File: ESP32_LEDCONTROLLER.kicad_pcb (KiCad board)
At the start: 2 copper layers, 17 parts, among them J1 ST-04, J2 ST-00, J3 ST-01, J4 ST-02, J5 ST-03, U1 LM2576HVT-5, U2 ESP32_NODEMCU

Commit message: v0.1 of the LED Controller has been completed.
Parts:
- added D1: D_Schottky, Diode_THT:D_DO-27_P12.70mm_Horizontal, F.Cu at (144.8, 109.2)
- added L1: L100, Inductor_THT:L_Radial_D9.5mm_P5.00mm_Fastron_07HVP, F.Cu at (134.6, 91.4)
- added U3: SN74LV4T125, Package_DIP:DIP-14_W7.62mm, F.Cu at (83.8, 110.5)
- C2: footprint Capacitor_THT:CP_Radial_D8.0mm_P3.50mm -> Capacitor_THT:CP_Radial_D10.0mm_P5.00mm
- R1, R2, R3, R4, R5, R6, R7, R8: footprint Resistor_THT:R_Axial_DIN0207_L6.3mm_D2.5mm_P2.54mm_Vertical -> Resistor_THT:R_Axial_DIN0207_L6.3mm_D2.5mm_P7.62mm_Horizontal
- U2: value ESP32_NODEMCU -> ESP32-DEVKIT-V1; footprint Esp32NodeMCU:MODULE_ESP32_NODEMCU -> ESP32-Devkitv1:MODULE_ESP32_DEVKIT_V1
- moved J5 161.1 mm to (85.1, 127.0), turned to -90 degrees
- moved J4 155.3 mm to (85.1, 116.8), turned to -90 degrees
- moved R7 131.8 mm to (99.1, 127.0), turned to 180 degrees
- moved R8 129.3 mm to (99.1, 132.1), turned to 180 degrees
- moved R5 128.5 mm to (99.1, 116.8), turned to 180 degrees
- moved R6 125.0 mm to (99.1, 121.9), turned to 180 degrees
- moved U2 88.7 mm to (116.8, 111.8), turned to 180 degrees
- moved J2 87.6 mm to (156.2, 132.1), turned to 90 degrees
- moved R2 86.2 mm to (142.2, 127.0)
- moved R3 86.2 mm to (142.2, 121.9)
- moved J3 85.6 mm to (156.2, 121.9)
- moved R1 83.6 mm to (142.2, 132.1)
- moved R4 80.7 mm to (142.2, 116.8)
- moved C2 46.8 mm to (139.7, 104.1)
- moved U1 30.6 mm to (147.3, 99.1), turned to 90 degrees
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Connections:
- R1 pad 1: Net-(U2-PadJ5_4) -> Net-(R1-Pad1)
- R2 pad 1: Net-(U2-PadJ5_2) -> Net-(R2-Pad1)
- R3 pad 1: Net-(U2-PadJ4_14) -> Net-(R3-Pad1)
- R4 pad 1: Net-(U2-PadJ4_13) -> Net-(R4-Pad1)
- U1 pad 2: VCC -> Net-(D1-Pad1)
- U1 pad 4: unconnected-(U1-Pad4) -> VCC
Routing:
- net VCC: track 0.00 -> 156.3 mm
- net Net-(R8-Pad1): track 0.00 -> 47.0 mm
- net Net-(R7-Pad1): track 0.00 -> 45.4 mm
- net Net-(U2-PadJ5_4): track 43.7 -> 0.00 mm
- net Net-(D1-Pad1): track 0.00 -> 41.3 mm
- net Net-(U2-PadJ5_2): track 40.1 -> 0.00 mm
- net Net-(U2-Pad22): track 0.00 -> 20.7 mm
- net Net-(U2-Pad24): track 0.00 -> 20.5 mm
- net VSS: track 0.00 -> 17.0 mm
- net Net-(R1-Pad1): track 0.00 -> 16.8 mm
- net Net-(R6-Pad1): track 0.00 -> 16.1 mm
- net Net-(R4-Pad1): track 0.00 -> 16.0 mm
- net Net-(R2-Pad1): track 0.00 -> 15.7 mm
- net Net-(U2-Pad23): track 0.00 -> 14.8 mm
- net Net-(R3-Pad1): track 0.00 -> 14.7 mm
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- added copper zone on F.Cu, net GND
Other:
- board outline added: 83.8 x 57.1 mm

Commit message: upload table
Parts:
- added G***: LOGO, table:table, F.Cu at (91.4, 92.7)

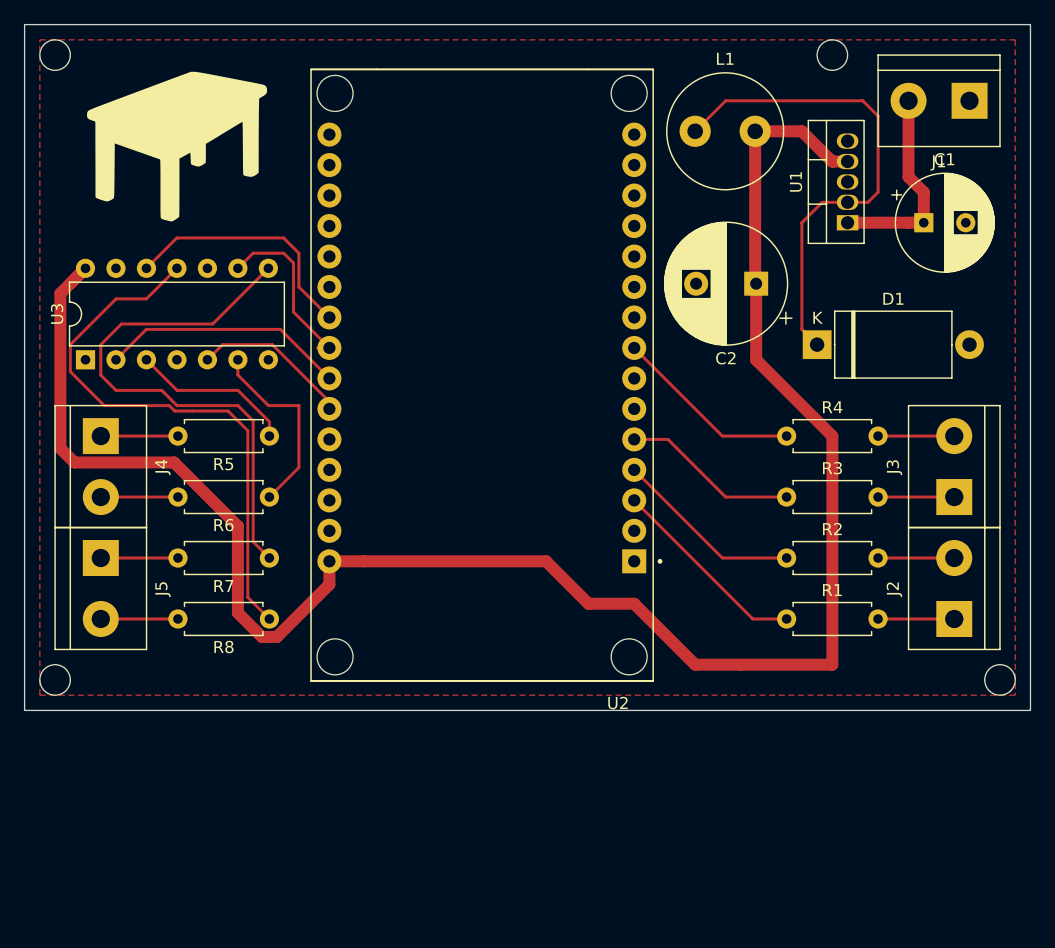
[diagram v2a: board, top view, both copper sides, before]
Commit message: Refactor by dropping level shifter & changing board layout
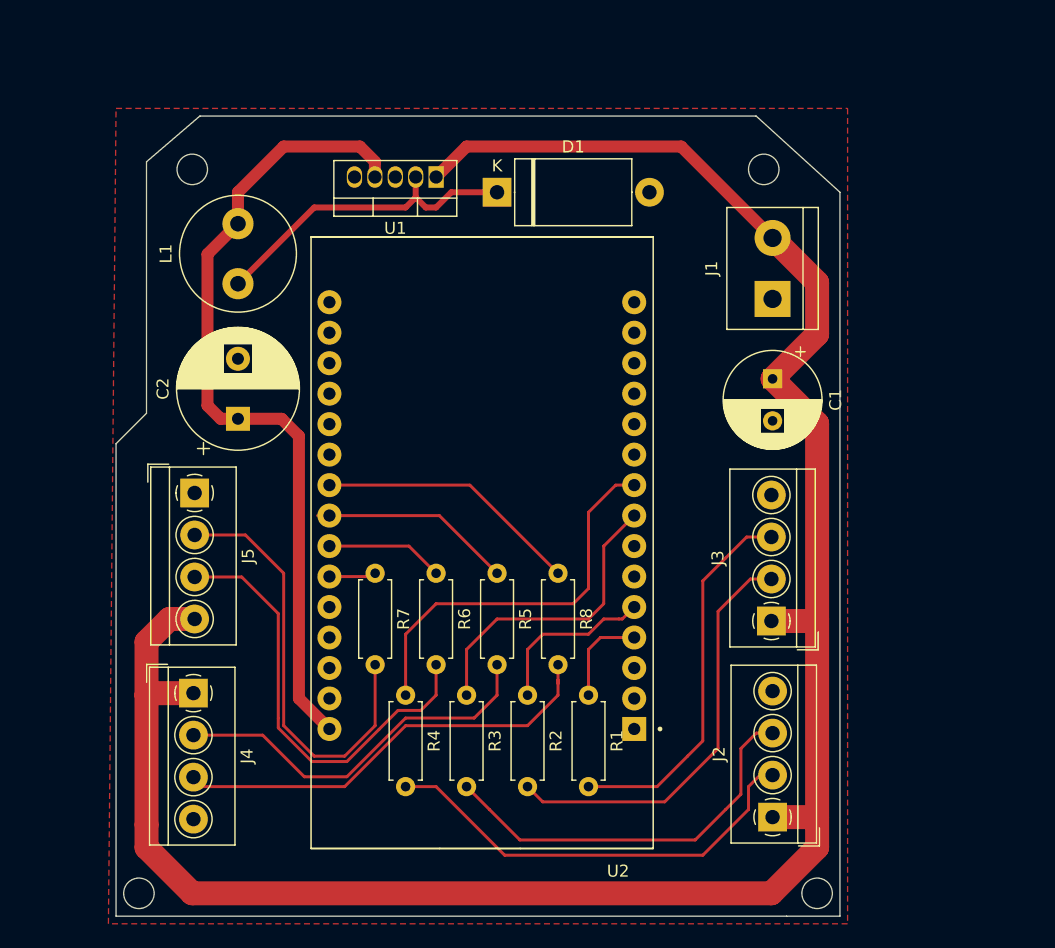
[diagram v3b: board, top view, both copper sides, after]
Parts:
- removed G***: LOGO, table:table
- removed U3: SN74LV4T125, Package_DIP:DIP-14_W7.62mm
- J2: value ST-00 -> Screw_Terminal_01x04; footprint TerminalBlock:TerminalBlock_bornier-2_P5.08mm -> TerminalBlock_4Ucon:TerminalBlock_4Ucon_1x04_P3.50mm_Horizontal
- J3: value ST-01 -> Screw_Terminal_01x04; footprint TerminalBlock:TerminalBlock_bornier-2_P5.08mm -> TerminalBlock_4Ucon:TerminalBlock_4Ucon_1x04_P3.50mm_Horizontal
- J4: value ST-02 -> Screw_Terminal_01x04; footprint TerminalBlock:TerminalBlock_bornier-2_P5.08mm -> TerminalBlock_4Ucon:TerminalBlock_4Ucon_1x04_P3.50mm_Horizontal
- J5: value ST-03 -> Screw_Terminal_01x04; footprint TerminalBlock:TerminalBlock_bornier-2_P5.08mm -> TerminalBlock_4Ucon:TerminalBlock_4Ucon_1x04_P3.50mm_Horizontal
- moved C2 44.6 mm to (96.5, 115.4), turned to 90 degrees
- moved L1 40.2 mm to (96.5, 104.1), turned to 90 degrees
- moved R4 38.4 mm to (110.5, 138.4), turned to -90 degrees
- moved U1 34.5 mm to (113.0, 95.2), turned to 180 degrees
- moved R3 31.4 mm to (115.6, 138.4), turned to -90 degrees
- moved D1 29.5 mm to (118.1, 96.5)
- moved R2 24.4 mm to (120.7, 138.4), turned to -90 degrees
- moved R8 24.3 mm to (123.2, 128.3), turned to -90 degrees
- moved J1 23.3 mm to (141.1, 105.4), turned to 90 degrees
- moved J4 22.8 mm to (92.8, 138.3)
- moved J2 22.4 mm to (141.1, 148.6)
- moved R5 22.1 mm to (118.1, 128.3), turned to -90 degrees
- moved J3 18.4 mm to (141.0, 132.2)
- moved C1 18.1 mm to (141.1, 112.1), turned to -90 degrees
- moved R1 17.7 mm to (125.7, 138.4), turned to -90 degrees
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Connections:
- J2 pad 1: Net-(J2-Pad1) -> VSS
- J3 pad 1: Net-(J3-Pad1) -> VSS
- J4 pad 1: Net-(J4-Pad1) -> VSS
- J5 pad 1: Net-(J5-Pad1) -> GND
- R1 pad 2: Net-(J2-Pad1) -> Net-(J3-Pad3)
- R2 pad 2: Net-(J2-Pad2) -> Net-(J3-Pad2)
- R3 pad 2: Net-(J3-Pad1) -> Net-(J2-Pad3)
- R4 pad 2: Net-(J3-Pad2) -> Net-(J2-Pad2)
- R5 pad 1: Net-(R5-Pad1) -> Net-(U2-Pad23)
- R5 pad 2: Net-(J4-Pad1) -> Net-(J4-Pad2)
- R6 pad 2: Net-(J4-Pad2) -> Net-(J5-Pad3)
- R7 pad 1: Net-(R7-Pad1) -> Net-(U2-Pad25)
- R7 pad 2: Net-(J5-Pad1) -> Net-(J5-Pad2)
- R8 pad 2: Net-(J5-Pad2) -> Net-(J4-Pad3)
- U2 pad 22: Net-(U2-Pad22) -> Net-(R8-Pad1)
- U2 pad 24: Net-(U2-Pad24) -> Net-(R6-Pad1)
- U2 pad 3: Net-(R1-Pad1) -> unconnected-(U2-Pad3)
- U2 pad 4: Net-(R2-Pad1) -> Net-(R1-Pad1)
- U2 pad 5: Net-(R3-Pad1) -> Net-(R2-Pad1)
- U2 pad 8: Net-(R4-Pad1) -> Net-(R3-Pad1)
- U2 pad 9: unconnected-(U2-Pad9) -> Net-(R4-Pad1)
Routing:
- net VSS: track 17.0 -> 180.2 mm
- net VCC: track 156.3 -> 67.8 mm
- net Net-(R7-Pad1): track 45.4 -> 0.00 mm
- net Net-(J5-Pad3): track 0.00 -> 36.9 mm
- net Net-(J4-Pad3): track 0.00 -> 36.7 mm
- net Net-(J2-Pad3): track 0.00 -> 33.3 mm
- net Net-(J3-Pad3): track 0.00 -> 31.7 mm
- net Net-(J2-Pad2): track 6.35 -> 37.3 mm
- net Net-(J5-Pad2): track 6.43 -> 36.2 mm
- net Net-(J3-Pad2): track 6.35 -> 35.2 mm
- net Net-(J4-Pad2): track 6.54 -> 32.1 mm
- net Net-(R8-Pad1): track 47.0 -> 22.1 mm
- net Net-(U2-Pad22): track 20.7 -> 0.00 mm
- net Net-(U2-Pad24): track 20.5 -> 0.00 mm
- net Net-(R4-Pad1): track 16.0 -> 33.0 mm
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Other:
- board size 83.8 x 57.1 mm -> 60.3 x 66.7 mm

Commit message: update & add gerbers
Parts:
- moved J2 4.01 mm to (137.1, 148.8)
- moved J1 3.92 mm to (137.2, 105.1)
- moved C1 3.92 mm to (137.2, 111.8)
- moved J3 3.81 mm to (137.2, 132.1)
- moved L1 3.59 mm to (99.1, 101.6), turned to 180 degrees
- moved J4 2.54 mm to (95.3, 138.1)
- moved J5 2.44 mm to (95.3, 121.6)
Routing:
- net VSS: track 180.2 -> 167.8 mm
- net Net-(J2-Pad2): track 37.3 -> 31.6 mm
- net Net-(D1-Pad1): track 27.1 -> 32.0 mm
- net Net-(J2-Pad3): track 33.3 -> 28.4 mm
- net Net-(J4-Pad3): track 36.7 -> 33.2 mm
- net Net-(J4-Pad2): track 32.1 -> 28.9 mm
- net Net-(J3-Pad2): track 35.2 -> 32.5 mm
- net Net-(J5-Pad3): track 36.9 -> 34.5 mm
- net Net-(J5-Pad2): track 36.2 -> 33.8 mm
- net Net-(J3-Pad3): track 31.7 -> 29.4 mm
- net Net-(U2-Pad23): track 17.0 -> 16.0 mm
- net Net-(U2-Pad25): track 4.52 -> 3.92 mm
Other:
- board size 60.3 x 66.7 mm -> 52.6 x 65.3 mm

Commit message: graphics & shitposting
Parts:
- added G***: LOGO, table:intersofia-pcb-info_neg, B.Cu at (116.9, 121.8)
- moved D1 17.9 mm to (135.9, 94.9), turned to -90 degrees
- moved J1 12.0 mm to (129.8, 95.6), turned to 180 degrees
- moved J5 1.93 mm to (97.3, 121.5)
- moved J4 1.91 mm to (97.3, 138.1)
- moved J2 0.13 mm to (137.1, 148.6)
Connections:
- J5 pad 1: GND -> VSS
- J5 pad 4: VSS -> GND
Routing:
- net VSS: track 167.8 -> 361.2 mm
- net Net-(D1-Pad1): track 32.0 -> 87.5 mm
- net VCC: track 67.8 -> 105.3 mm
- net Net-(J4-Pad3): track 33.2 -> 31.3 mm
- net Net-(J4-Pad2): track 28.9 -> 27.0 mm
- net Net-(J5-Pad2): track 33.8 -> 32.3 mm
- net Net-(J5-Pad3): track 34.5 -> 33.7 mm
- added copper zone on B.Cu, net GND
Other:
- board size 52.6 x 65.3 mm -> 51.8 x 65 mm
- board text added: "1 ч. синьо 1 ч. зелено 1 ч. червено 1 бр. ESP32-DevKit-V1 1-3000 бр. WS2815 на вкус 1 бр. Дросел 2 бр. Кондензатор 1 бр. WLED Firmware"
- board text added: "12V"
- board text added: "D1"
- board text added: "D2"
- board text added: "GND"
- board text added: "JLCJLCJLCJLC"
- board text added: "Запоете компонентите и оставяте в хладилника за около 5 минути. Насладете се на Вашето R G B"
- board text added: "ИнтерСофия RGB"
